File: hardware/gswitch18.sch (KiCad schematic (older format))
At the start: 21 parts, among them IC1 ATMEGA88P, P1 CONN_6X2, P2 CONN_6X2, P3 CONN_6X2, P4 USB, P5 ISP x48, X1 12MHz

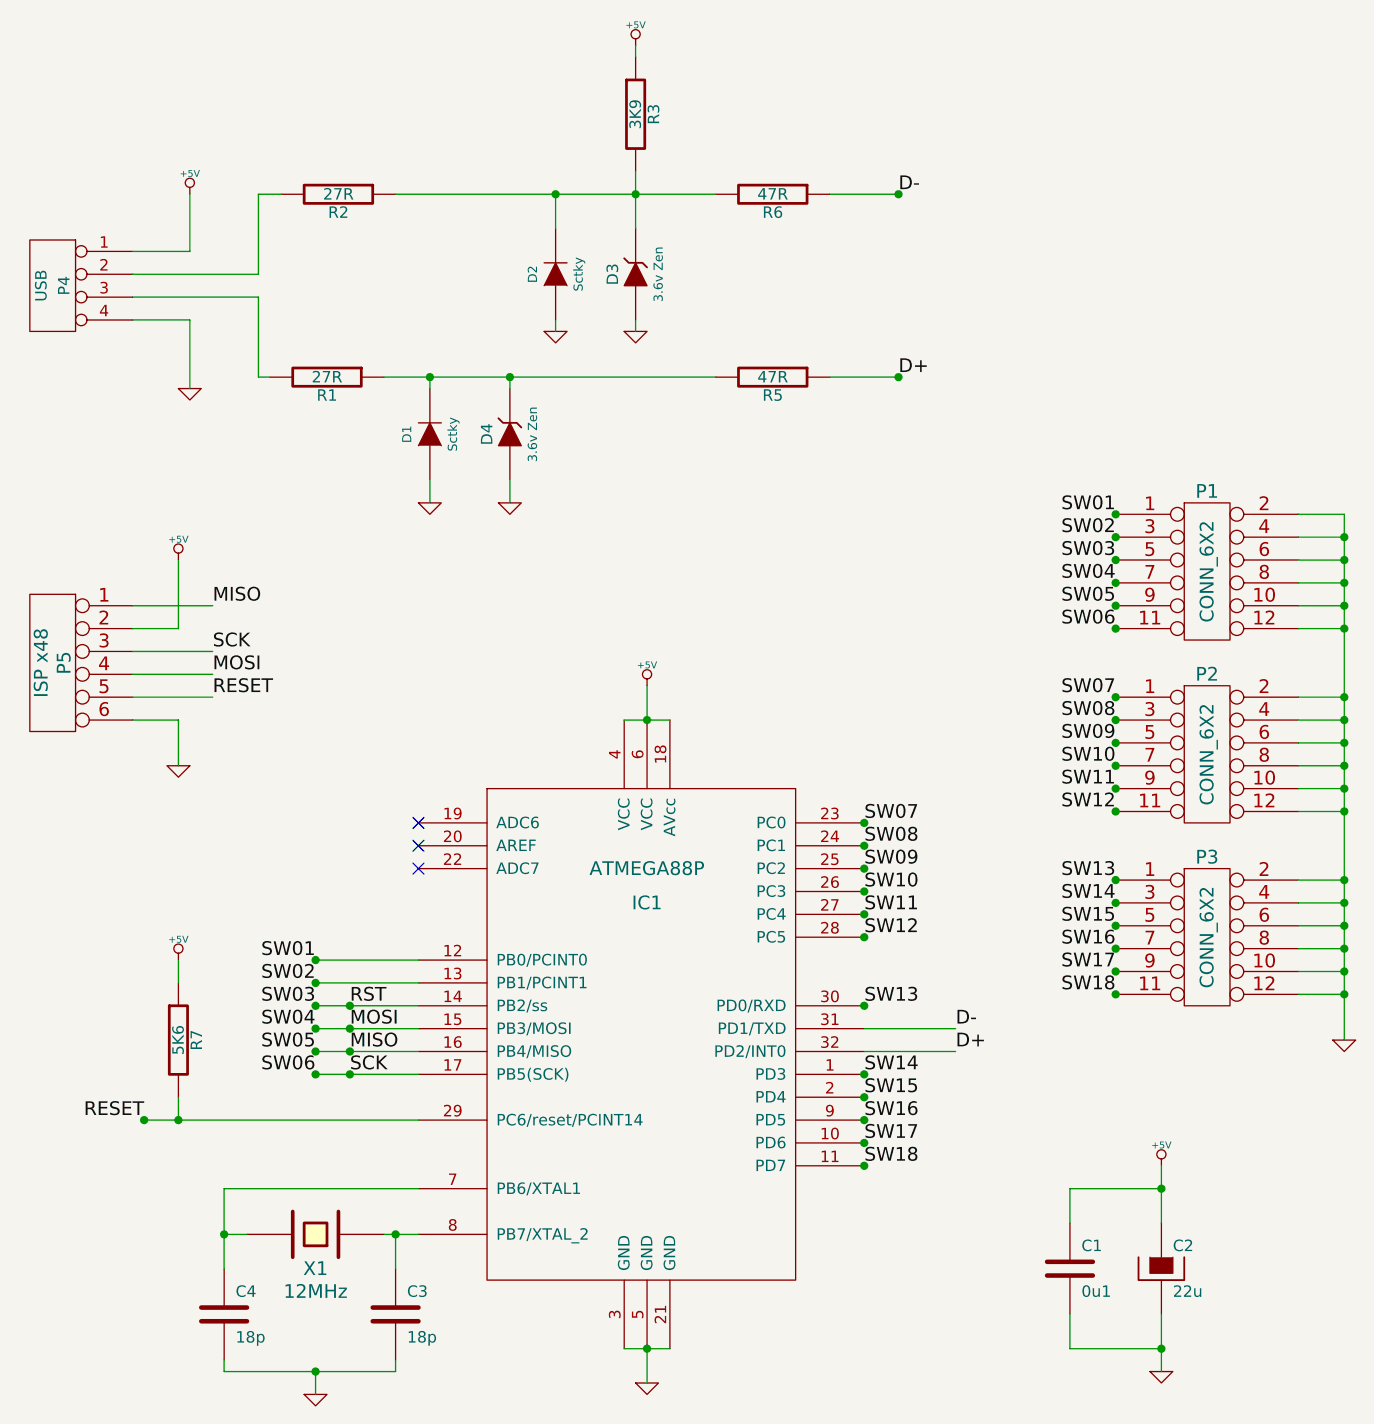
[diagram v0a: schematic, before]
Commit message: Version 1.0 prototype tested working. [MILESTONE]
Firmware modified for ATmega88p. Debugged and tested OK.
(Old [main].c etc backed up to [etc]-2560.*)

There were some errors with the PCB design around the
USB socket ground pin and the front silk-screen switch 
number labels.
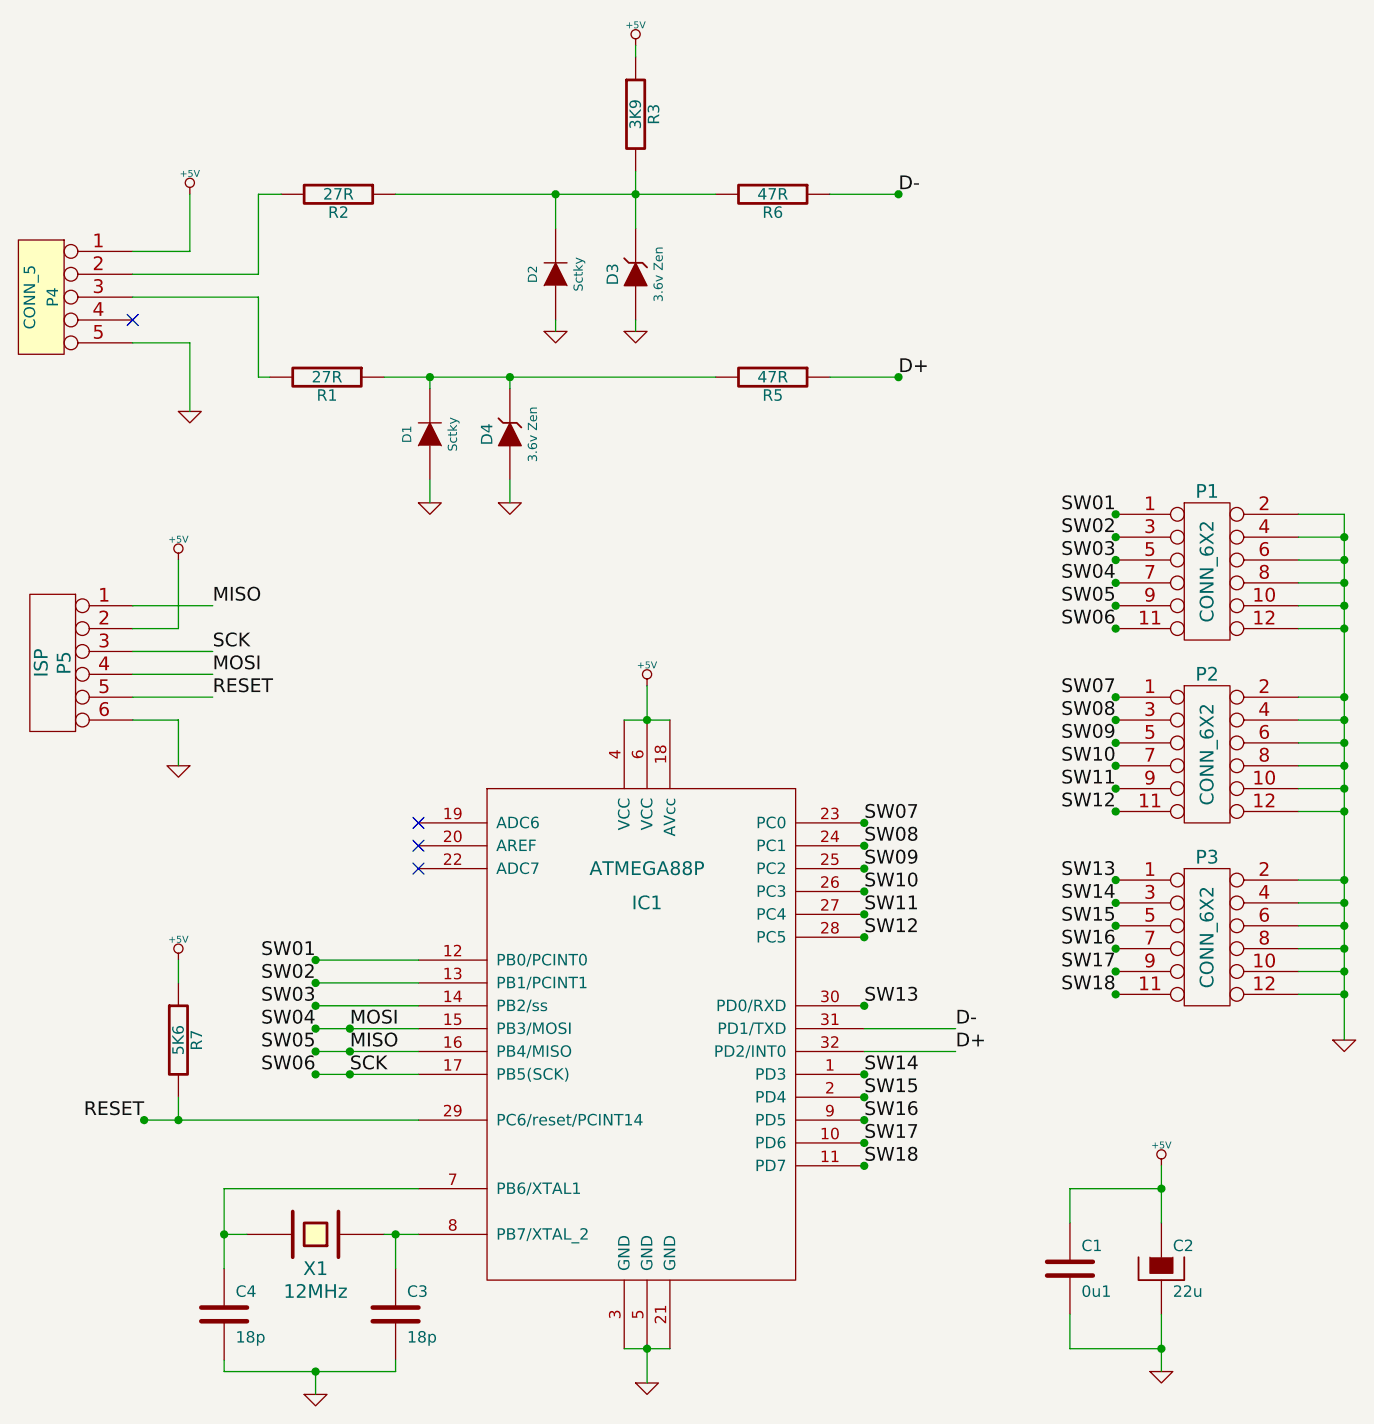
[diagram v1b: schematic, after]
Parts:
- removed P4: USB, symbol CONN_4
- added P4: CONN_5, symbol CONN_5
- P5: value ISP x48 -> ISP
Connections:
- net +5V: now also P4.1
- net GND: now also P4.5
- net at R2.2: now also P4.2
- net at R1.2: now also P4.3
- net RST renamed SW03
- no-connect marks 3 -> 4

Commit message: Decided to match PCB design and code to prototype PCB silk screen, so as not to waste several boards.
This should be the final v1.0 version now, since everything
appears to be working and labelled correctly on the board.

Yay \o/

(Also added some wiki images with this commit.)
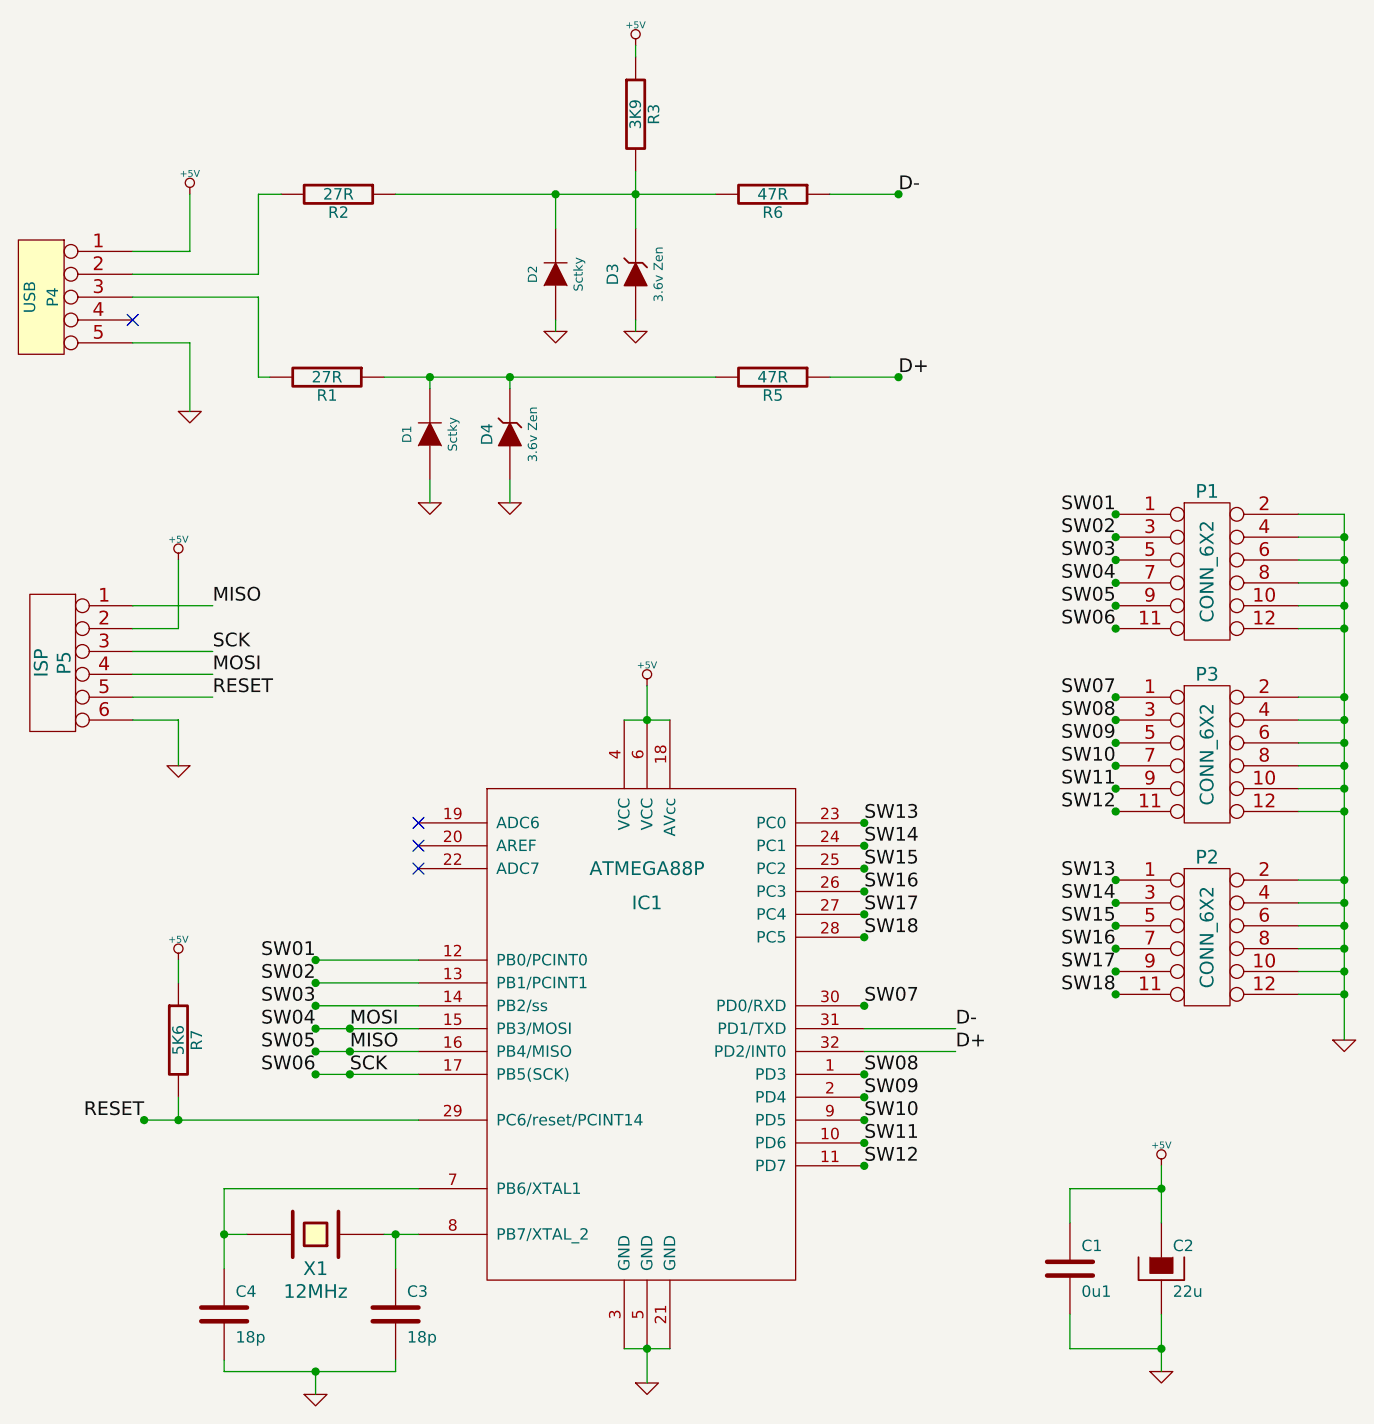
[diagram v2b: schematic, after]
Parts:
- P4: value CONN_5 -> USB
- renumbered P3 to P2, P2 to P3
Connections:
- net SW07: now also IC1.30 (PD0/RXD); no longer IC1.23 (PC0)
- net SW08: now also IC1.1 (PD3); no longer IC1.24 (PC1)
- net SW09: now also IC1.2 (PD4); no longer IC1.25 (PC2)
- net SW10: now also IC1.9 (PD5); no longer IC1.26 (PC3)
- net SW11: now also IC1.10 (PD6); no longer IC1.27 (PC4)
- net SW12: now also IC1.11 (PD7); no longer IC1.28 (PC5)
- net SW13: now also IC1.23 (PC0); no longer IC1.30 (PD0/RXD)
- net SW14: now also IC1.24 (PC1); no longer IC1.1 (PD3)
- net SW15: now also IC1.25 (PC2); no longer IC1.2 (PD4)
- net SW16: now also IC1.26 (PC3); no longer IC1.9 (PD5)
- net SW17: now also IC1.27 (PC4); no longer IC1.10 (PD6)
- net SW18: now also IC1.28 (PC5); no longer IC1.11 (PD7)
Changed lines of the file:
@@
-EESchema Schematic File Version 2  date Tue 25 Sep 2012 08:28:44 PM NZST
+EESchema Schematic File Version 2  date Wed 26 Sep 2012 08:32:34 AM NZST
 LIBS:power
 LIBS:device
@@
 P 1400 2000
 F 0 "P4" V 1350 2000 50  0000 C CNN
-F 1 "CONN_5" V 1450 2000 50  0000 C CNN
+F 1 "USB" V 1450 2000 50  0000 C CNN
 	1    1400 2000
 	-1   0    0    -1
 $EndComp
 $Comp
-L CONN_6X2 P3
+L CONN_6X2 P2
 U 1 1 504B1B34
 P 6500 4800
-F 0 "P3" H 6500 5150 60  0000 C CNN
+F 0 "P2" H 6500 5150 60  0000 C CNN
 F 1 "CONN_6X2" V 6500 4800 60  0000 C CNN
 	1    6500 4800
@@
 $EndComp
 $Comp
-L CONN_6X2 P2
+L CONN_6X2 P3
 U 1 1 504B1AC6
 P 6500 4000
-F 0 "P2" H 6500 4350 60  0000 C CNN
+F 0 "P3" H 6500 4350 60  0000 C CNN
 F 1 "CONN_6X2" V 6500 4000 60  0000 C CNN
 	1    6500 4000
@@
 Text Label 6100 2950 2    60   ~ 0
 SW01
+Text Label 5000 4800 0    60   ~ 0
+SW18
+Text Label 5000 4700 0    60   ~ 0
+SW17
+Text Label 5000 4600 0    60   ~ 0
+SW16
+Text Label 5000 4500 0    60   ~ 0
+SW15
+Text Label 5000 4400 0    60   ~ 0
+SW14
+Text Label 5000 4300 0    60   ~ 0
+SW13
 Text Label 5000 5800 0    60   ~ 0
-SW18
+SW12
 Text Label 5000 5700 0    60   ~ 0
-SW17
+SW11
 Text Label 5000 5600 0    60   ~ 0
-SW16
+SW10
 Text Label 5000 5500 0    60   ~ 0
-SW15
+SW09
 Text Label 5000 5400 0    60   ~ 0
-SW14
+SW08
 Text Label 5000 5100 0    60   ~ 0
-SW13
-Text Label 5000 4800 0    60   ~ 0
-SW12
-Text Label 5000 4700 0    60   ~ 0
-SW11
-Text Label 5000 4600 0    60   ~ 0
-SW10
-Text Label 5000 4500 0    60   ~ 0
-SW09
-Text Label 5000 4400 0    60   ~ 0
-SW08
-Text Label 5000 4300 0    60   ~ 0
 SW07
 Text Label 2600 5400 2    60   ~ 0
